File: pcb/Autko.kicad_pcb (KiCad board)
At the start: 2 copper layers, 140 x 153 mm, 131 parts, among them J1 PDI, M1 LEFT, M2 RIGHT, Q1 Si4368DY, Q2 BC817, SW1 POWER, SW2 START, SW3 STOP, U1 LTC3872, U10 CNY70, U11 TB6612FNG, U12 RN4678, U2 TLV1117-33, U3 ATxmega16A4U-A, U4 CNY70, U5 CNY70, U6 CNY70, U7 CNY70, U8 CNY70, U9 CNY70, Y1 8MHz

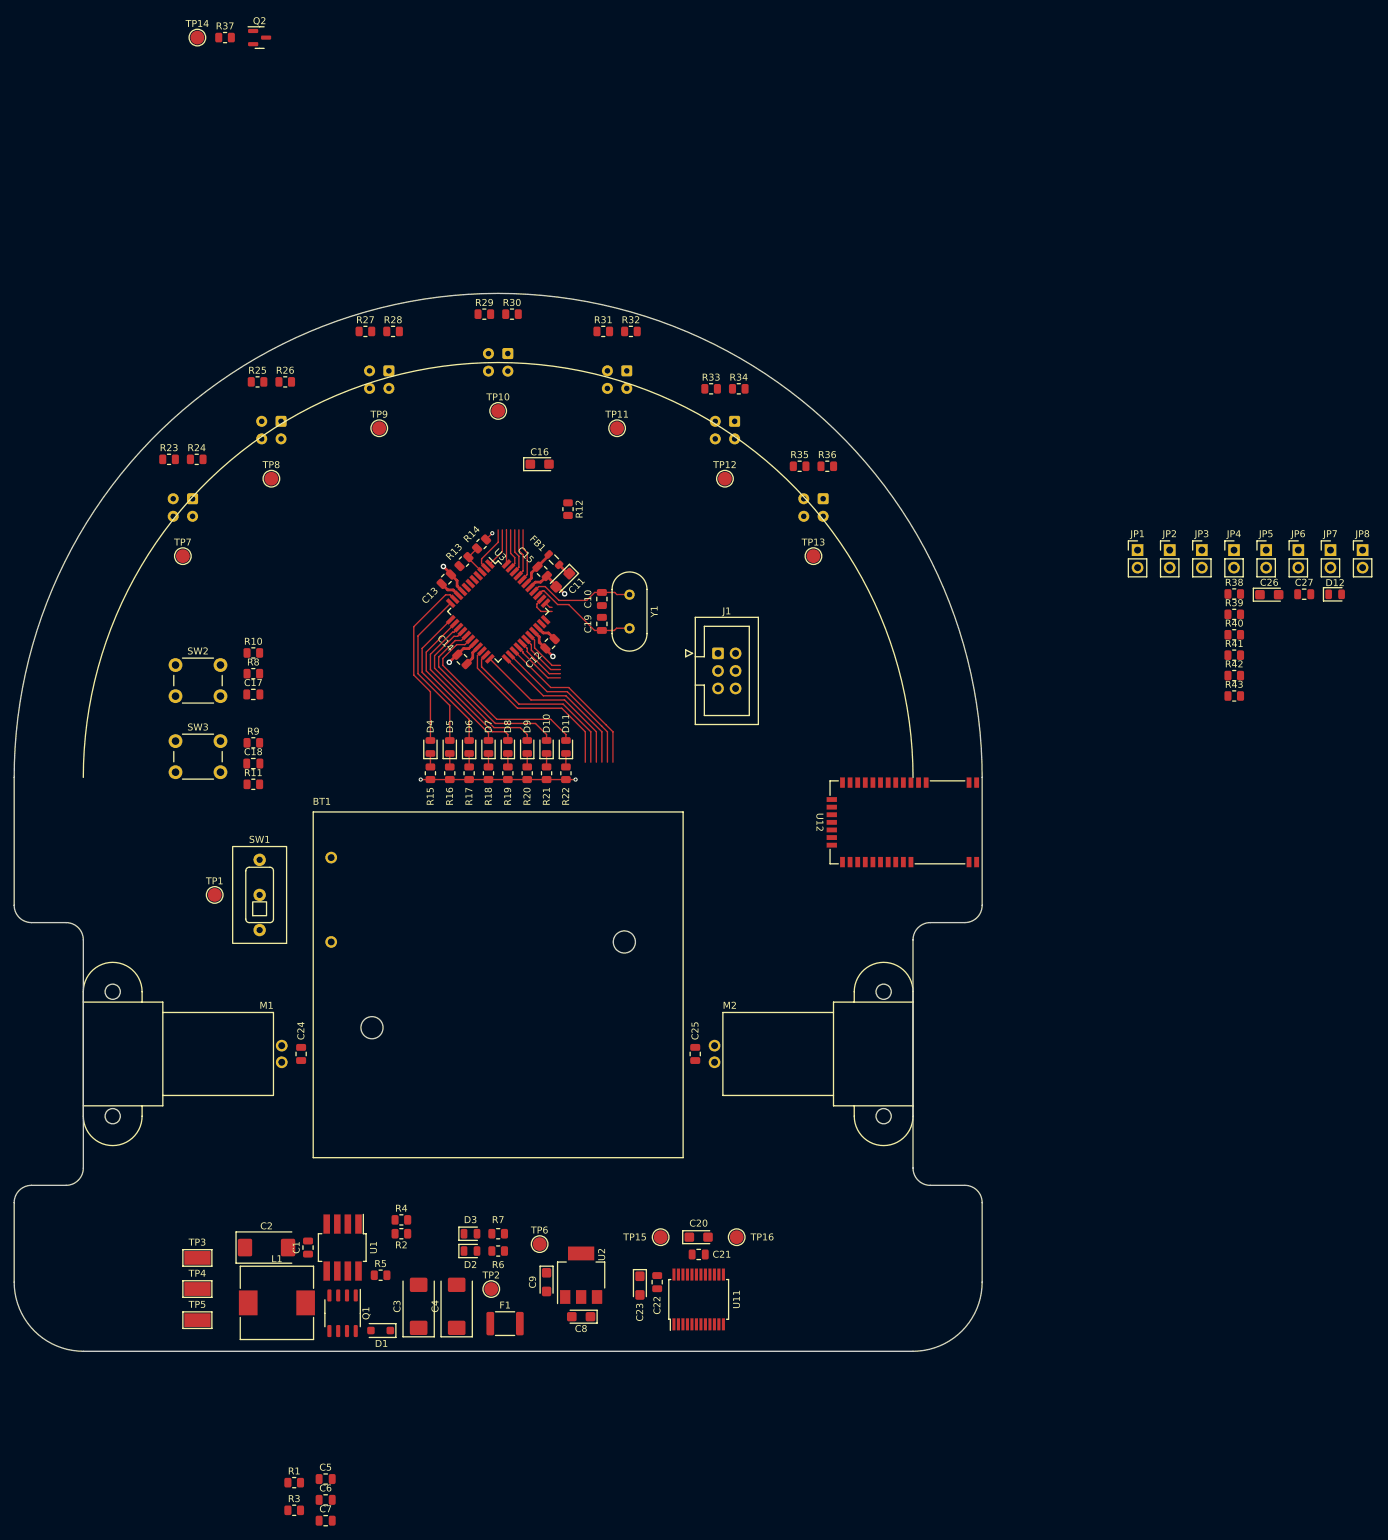
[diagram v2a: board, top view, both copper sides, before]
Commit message: [pcb] Trying to minimize number of vias
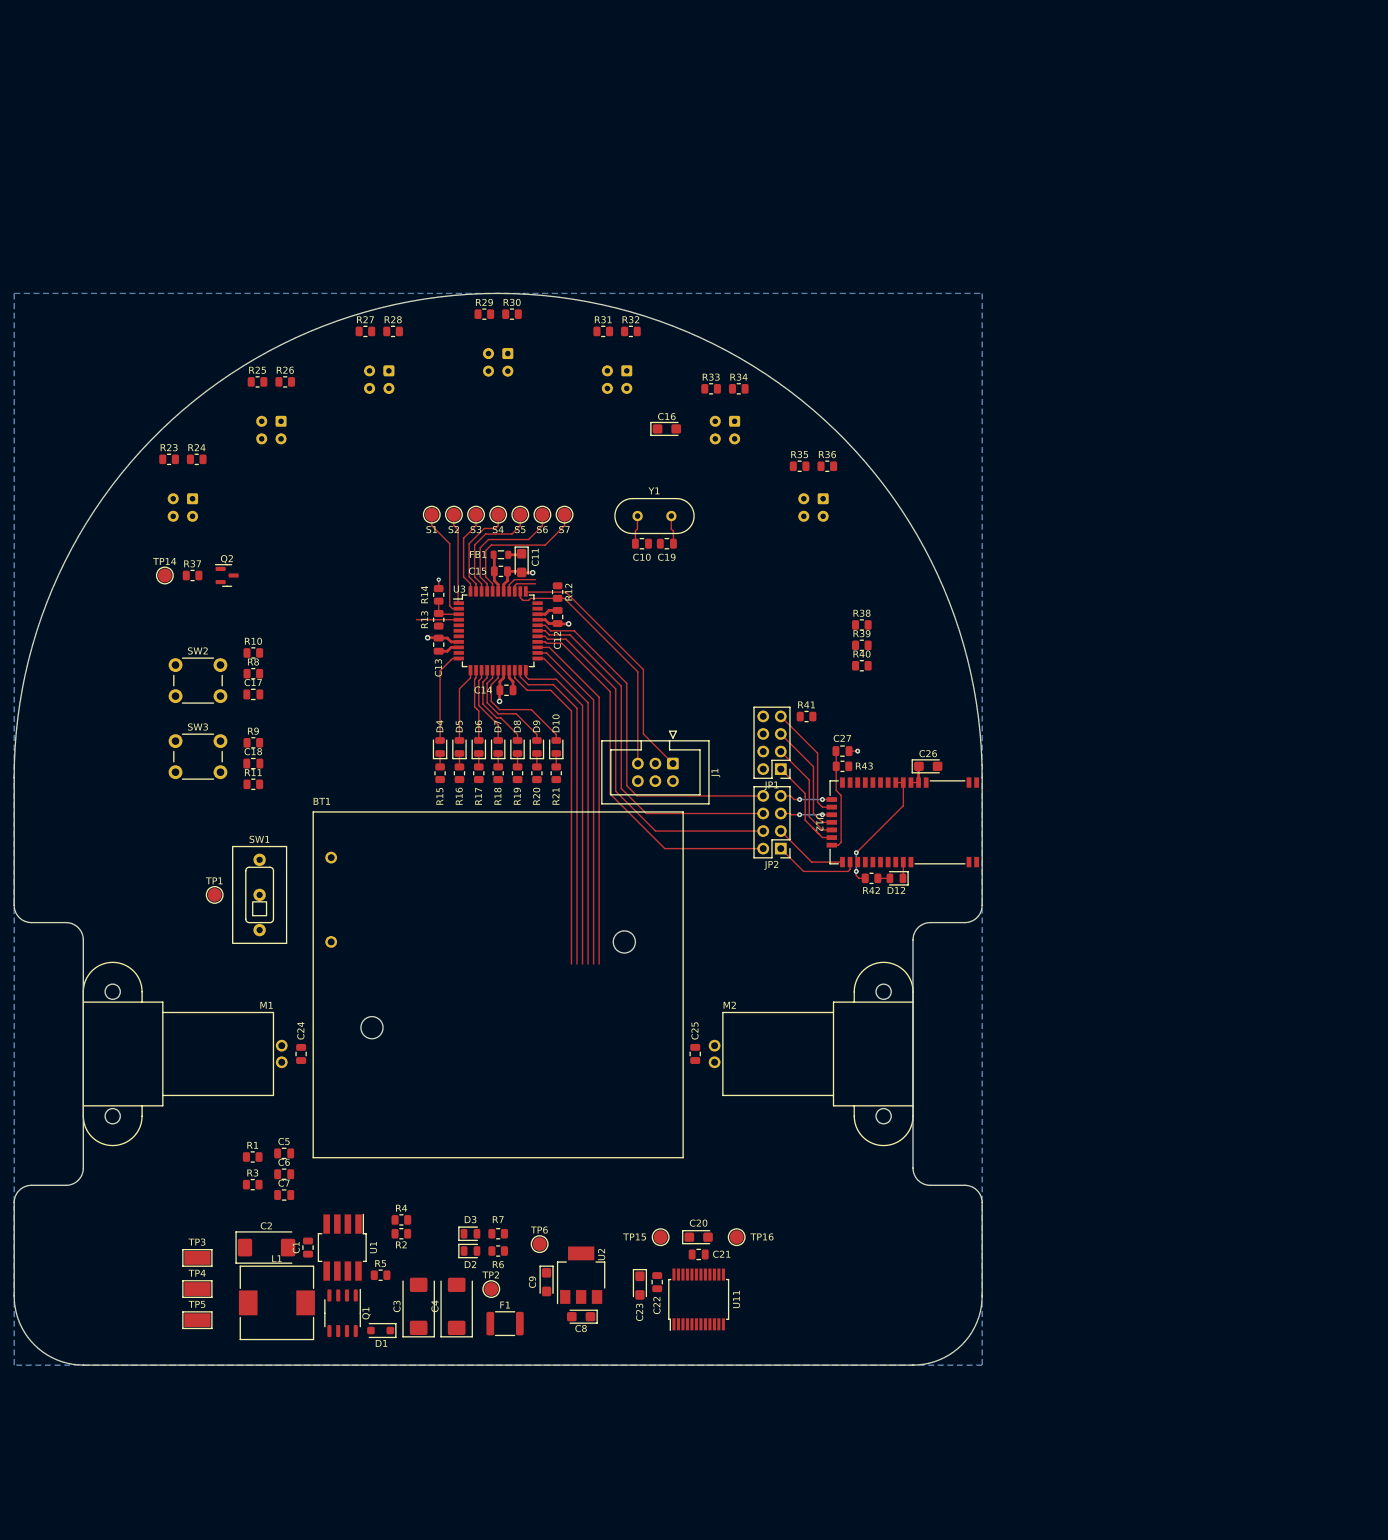
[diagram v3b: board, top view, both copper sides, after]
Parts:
- removed D11: YELLOW, LED_SMD:LED_0805_2012Metric
- removed JP3, JP4, JP5, JP6, JP7, JP8: Jumper_2_Bridged, Connector_PinHeader_2.54mm:PinHeader_1x02_P2.54mm_Vertical
- removed R22: ???R, Resistor_SMD:R_0805_2012Metric
- JP1, JP2: value Jumper_2_Bridged -> Jumper_x4_Bridged; footprint Connector_PinHeader_2.54mm:PinHeader_1x02_P2.54mm_Vertical -> Connector_PinHeader_2.54mm:PinHeader_2x04_P2.54mm_Vertical
- moved Q2 77.9 mm to (60.3, 71.3)
- moved R37 77.9 mm to (55.3, 71.3)
- moved TP14 77.9 mm to (51.3, 71.3)
- moved D12 75.6 mm to (157.1, 115.1), turned to 180 degrees
- moved JP2 70.9 mm to (140.4, 110.8), turned to 180 degrees
- moved C27 70.5 mm to (149.3, 96.7)
- moved R41 62.5 mm to (144.1, 91.7)
- moved JP1 60.5 mm to (140.4, 99.3), turned to 180 degrees
- moved R42 60.1 mm to (153.5, 115.1), turned to 180 degrees
- moved R43 57.6 mm to (149.3, 98.9), turned to 180 degrees
- moved C26 55.2 mm to (161.7, 98.9)
- moved R38 54.0 mm to (152.1, 78.5)
- moved R39 54.0 mm to (152.1, 81.4)
- moved R40 54.0 mm to (152.1, 84.3)
- moved C6 47.5 mm to (68.5, 157.9)
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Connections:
- JP1 pad 1: /Bluetooth/P2_0 -> /Bluetooth/EAN
- JP1 pad 2: +3.3V -> GND
- JP2 pad 1: /Bluetooth/P2_4 -> Net-(U12-UART_TX)
- JP2 pad 2: +3.3V -> /Bluetooth/TX
- U12 pad 15: Net-(JP8-A) -> Net-(U12-P1_7/CTS)
- U12 pad 17: Net-(JP7-A) -> Net-(U12-P0_0/RTS)
- U12 pad 22: Net-(JP6-A) -> Net-(U12-UART_RX)
- U12 pad 23: Net-(JP5-A) -> Net-(U12-UART_TX)
- U3 pad 10: /Microcontroller/LED1 -> unconnected-(U3-PC0-Pad10)
- U3 pad 11: /Microcontroller/LED2 -> /Microcontroller/LED1
- U3 pad 12: /Microcontroller/LED3 -> /Microcontroller/LED2
- U3 pad 13: /Microcontroller/LED4 -> /Microcontroller/LED3
- U3 pad 14: /Microcontroller/LED5 -> /Microcontroller/LED4
- U3 pad 15: /Microcontroller/LED6 -> /Microcontroller/LED5
- U3 pad 16: /Microcontroller/LED7 -> /Microcontroller/LED6
- U3 pad 17: /Microcontroller/LED8 -> /Microcontroller/LED7
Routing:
- net /Bluetooth/TX: track 8.02 -> 53.7 mm
- net /Bluetooth/RX: track 7.63 -> 53.0 mm
- net /Bluetooth/RTS: track 7.25 -> 52.2 mm
- net /Bluetooth/CTS: track 6.86 -> 51.5 mm
- net /Microcontroller/PDI_DATA: track 1.19 -> 37.1 mm
- net /Microcontroller/PDI_CLK: track 3.90 -> 35.8 mm
- net /Microcontroller/LED8: track 28.9 -> 0.00 mm
- net /Microcontroller/M2_PWM: track 23.5 -> 50.5 mm
- net /Microcontroller/M2_IN2: track 23.0 -> 49.1 mm
- net /Microcontroller/M2_IN1: track 22.6 -> 47.8 mm
- net /Microcontroller/M1_IN1: track 24.2 -> 48.2 mm
- net /Microcontroller/M1_IN2: track 26.1 -> 48.0 mm
- net /Microcontroller/M1_PWM: track 26.6 -> 47.9 mm
- net GND: track 44.8 -> 23.6 mm, vias 7 -> 6
- net /Bluetooth/BT_3V3: track 0.00 -> 18.8 mm, vias 0 -> 2
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- added copper zone on B.Cu, net GND
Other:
- board size 140 x 153 mm -> 140 x 155 mm

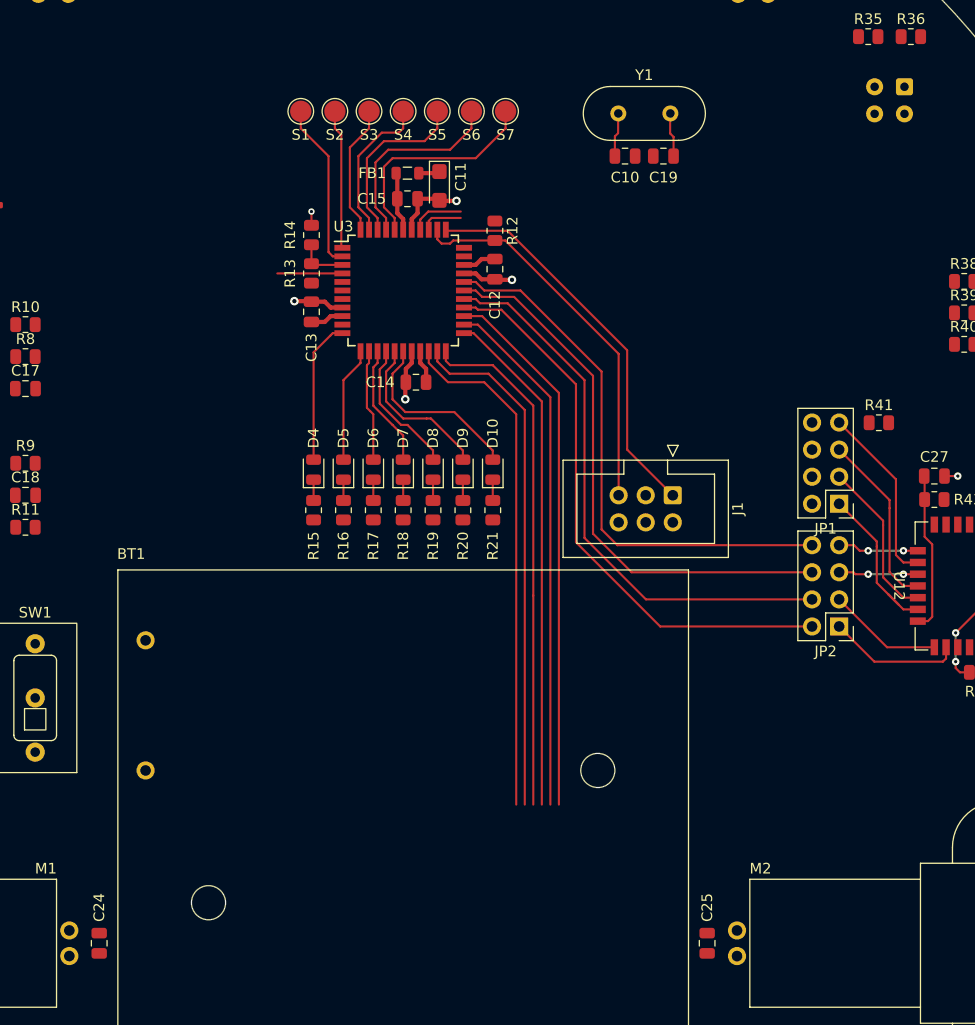
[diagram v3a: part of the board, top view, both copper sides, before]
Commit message: [pcb] Route PDI and UART
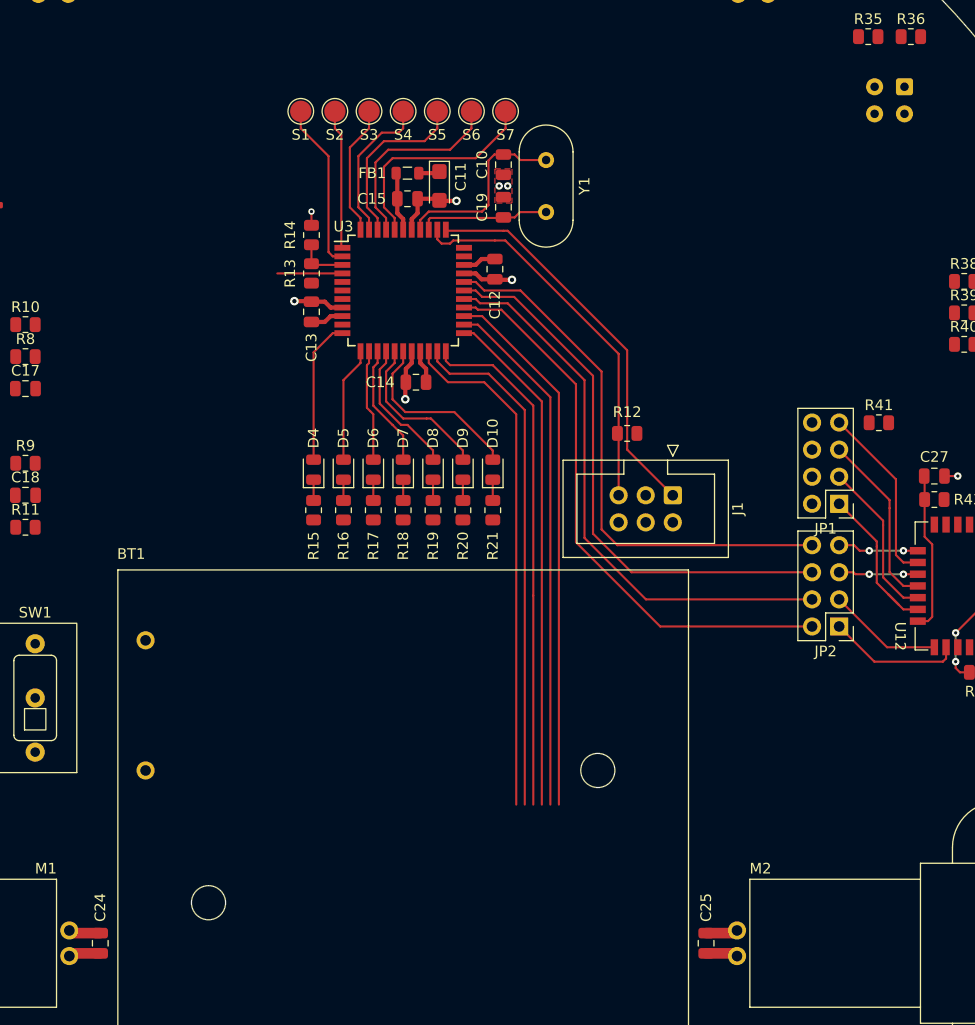
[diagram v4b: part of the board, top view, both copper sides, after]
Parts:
- moved R12 22.7 mm to (120.5, 92.7), turned to 180 degrees
- moved C19 15.7 mm to (108.9, 71.5), turned to 90 degrees
- moved Y1 14.9 mm to (112.9, 72.0), turned to 90 degrees
- moved C10 11.4 mm to (108.9, 67.5), turned to -90 degrees
- moved C24 0.10 mm to (71.1, 140.5)
- moved C25 0.10 mm to (127.9, 140.5)
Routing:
- net /Microcontroller/XTAL1: track 9.18 -> 17.9 mm
- net /Microcontroller/XTAL2: track 8.07 -> 12.2 mm
- net Net-(M2--): track 0.00 -> 3.00 mm
- net Net-(M2-+): track 0.00 -> 3.00 mm
- net Net-(M1--): track 0.00 -> 3.00 mm
- net Net-(M1-+): track 0.00 -> 3.00 mm
- net GND: vias 6 -> 8
- added copper zone on F.Cu, net GND
